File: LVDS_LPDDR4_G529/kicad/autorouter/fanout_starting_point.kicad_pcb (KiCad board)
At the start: 10 copper layers, 200 x 125 mm, 8 parts, among them IC1 ADC12DL500ACF_Aligned, U1 MT53D512M16D1DS_Aligned, U2 FT601Q_Aligned, U3 Ti90G529_Functions

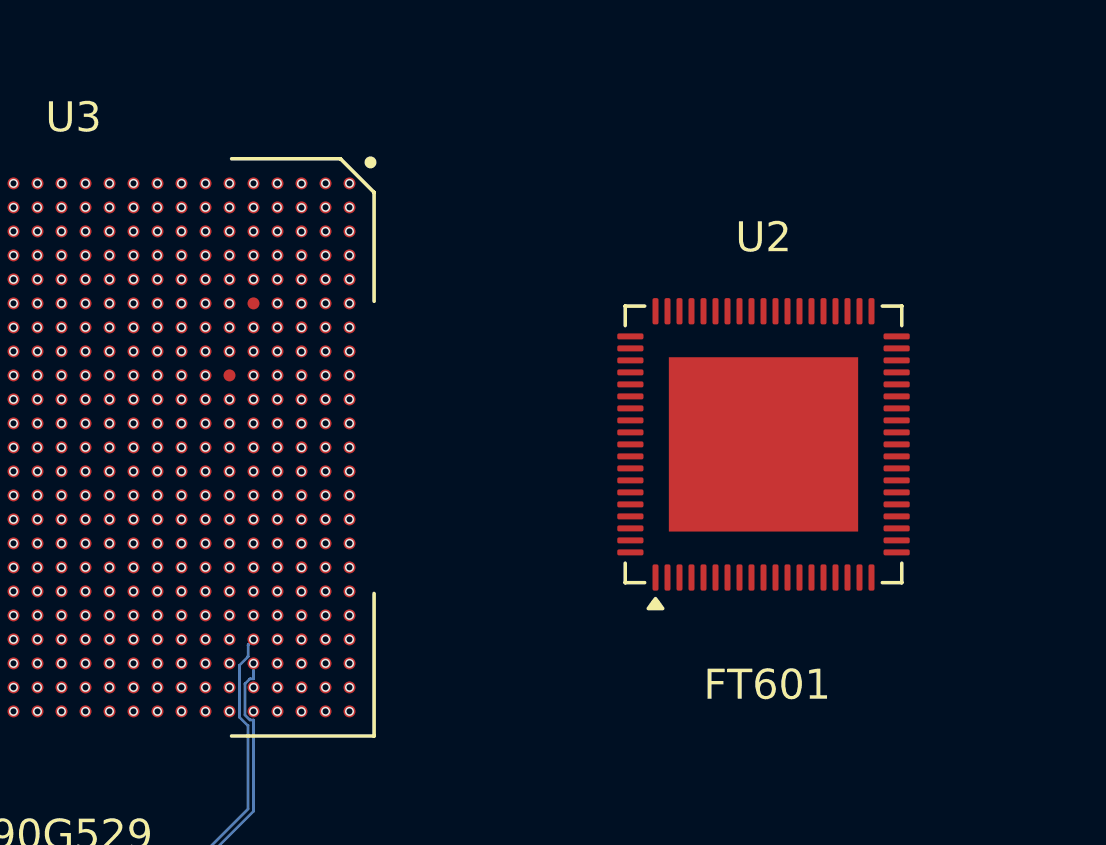
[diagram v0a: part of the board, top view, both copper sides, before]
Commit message: Working for 12 tracks, added README
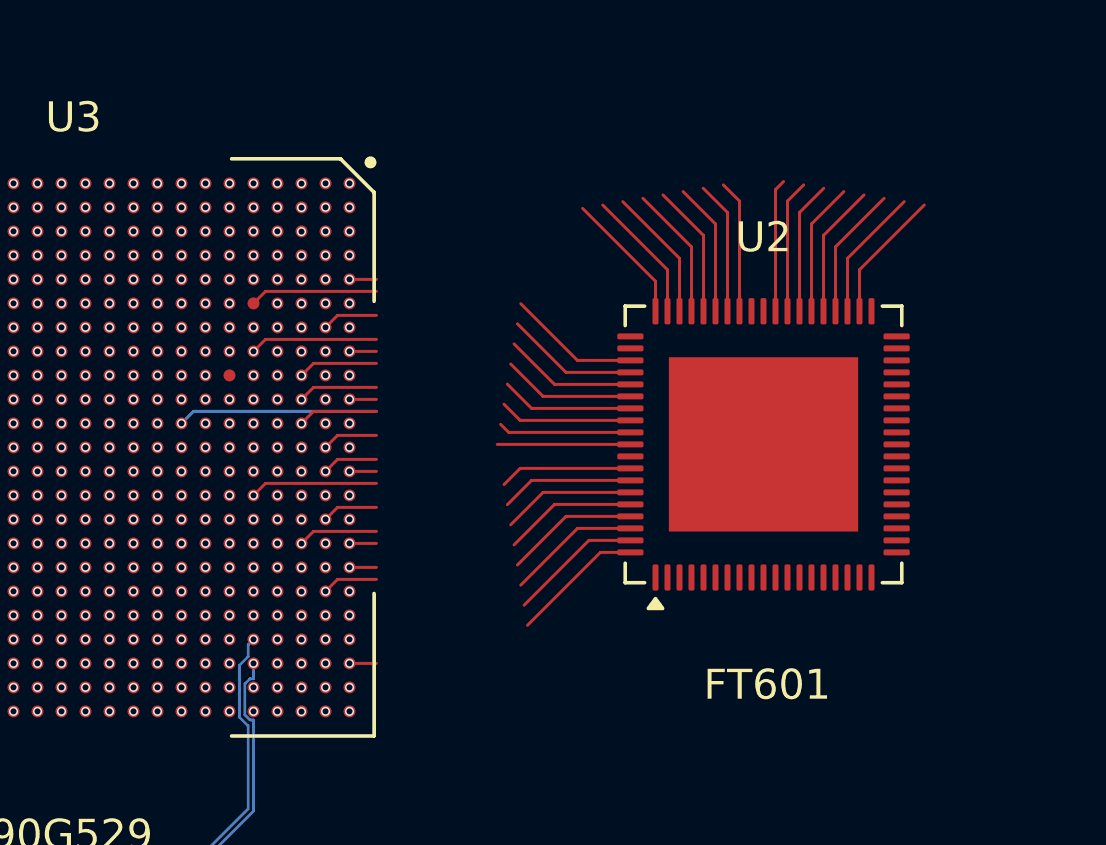
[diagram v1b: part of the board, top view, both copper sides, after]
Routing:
- net Net-(U2A-DATA_20): track 0.00 -> 11.1 mm
- net Net-(U2A-DATA_11): track 0.00 -> 11.1 mm
- net Net-(U2A-DATA_23): track 0.00 -> 10.3 mm
- net Net-(U2A-DATA_14): track 0.00 -> 10.3 mm
- net Net-(U2A-DATA_17): track 0.00 -> 10.3 mm
- net Net-(U2A-DATA_22): track 0.00 -> 9.50 mm
- net Net-(U2A-DATA_0): track 0.00 -> 9.50 mm
- net Net-(U2A-DATA_9): track 0.00 -> 8.70 mm
- net Net-(U2A-DATA_5): track 0.00 -> 8.70 mm
- net Net-(U2A-DATA_8): track 0.00 -> 8.70 mm
- net Net-(U2A-DATA_24): track 0.00 -> 8.70 mm
- net Net-(U2A-DATA_16): track 0.00 -> 8.70 mm
- net Net-(U2A-DATA_2): track 0.00 -> 8.70 mm
- net Net-(U2A-DATA_18): track 0.00 -> 7.90 mm
- net Net-(U2A-DATA_7): track 0.00 -> 7.10 mm
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
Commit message: better pattern
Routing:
- net Net-(U2A-DATA_23): track 10.3 -> 6.60 mm
- net Net-(U2A-DATA_22): track 9.50 -> 6.07 mm
- net Net-(U2A-DATA_7): track 7.10 -> 3.77 mm
- net Net-(U2A-DATA_8): track 8.70 -> 5.53 mm
- net Net-(U2A-DATA_6): track 5.34 -> 2.27 mm
- net Net-(U2A-DATA_24): track 8.70 -> 5.64 mm
- net Net-(U2A-DATA_21): track 6.30 -> 3.24 mm
- net Net-(U2A-DATA_9): track 8.70 -> 5.80 mm
- net Net-(U2A-DATA_20): track 11.1 -> 8.20 mm
- net unconnected-(U2C-VCC33-Pad38): track 0.00 -> 2.84 mm
- net unconnected-(U2C-VCC33-Pad20): track 0.00 -> 2.84 mm
- net unconnected-(U2C-DV10-Pad39): track 0.00 -> 2.84 mm
- net Net-(U2A-CLK): track 0.00 -> 2.84 mm
- net unconnected-(U2C-GND-Pad19): track 0.00 -> 2.84 mm
- net unconnected-(U2C-GND-Pad1): track 0.00 -> 2.84 mm
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
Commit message: Can add / remove vias during bga fanout
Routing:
- net /fpga_adc/lvds_rx1_1_N: track 72.3 -> 0.00 mm, vias 2 -> 0
- net /fpga_adc/lvds_rx1_1_P: track 72.2 -> 0.00 mm, vias 2 -> 0
- net unconnected-(IC1F-VLVDS_8-PadJ13): vias 1 -> 0
- net unconnected-(IC1F-VLVDS_7-PadJ12): vias 1 -> 0
- net unconnected-(IC1F-VLVDS_5-PadH13): vias 1 -> 0
- net unconnected-(IC1F-VLVDS_4-PadH12): vias 1 -> 0
- net unconnected-(IC1F-VLVDS_2-PadG12): vias 1 -> 0
- net unconnected-(IC1F-VLVDS_10-PadK12): vias 1 -> 0
- net unconnected-(IC1F-DGND_9-PadH14): vias 1 -> 0
- net unconnected-(IC1F-DGND_18-PadT16): vias 1 -> 0
- net unconnected-(IC1F-DGND_17-PadT15): vias 1 -> 0
- net unconnected-(IC1F-DGND_12-PadJ14): vias 1 -> 0
- net /fpga_adc/lvds_rx_top_clkin4_P: vias 2 -> 1
- net /fpga_adc/lvds_rx_top_clkin4_N: vias 2 -> 1
- net /fpga_adc/lvds_rx_top_clkin2_P: vias 2 -> 1
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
